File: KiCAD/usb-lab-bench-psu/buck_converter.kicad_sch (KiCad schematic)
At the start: 14 parts, among them U14 LMR16006X

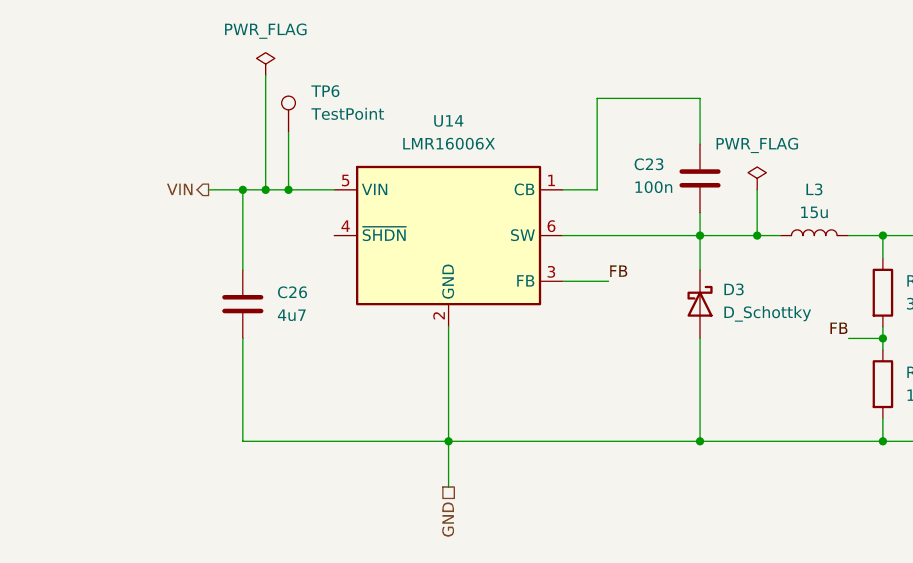
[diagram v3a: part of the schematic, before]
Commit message: restructured schematics to better show individual boards
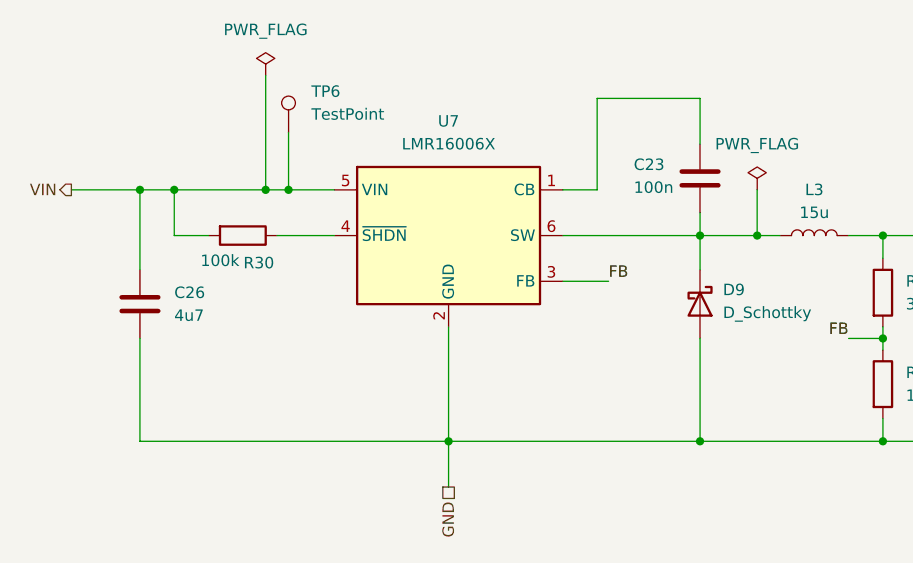
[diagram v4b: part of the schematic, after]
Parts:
- added R30: 100k, Resistor_SMD:R_0402_1005Metric_Pad0.72x0.64mm_HandSolder, symbol Device:R
- renumbered D3 to D9, U14 to U7
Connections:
- net VIN: now also R30.2
- net at U7.4 (~{SHDN}): now also R30.1
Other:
- moved on the sheet: C26
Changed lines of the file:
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@@
 	(paper "A4")
+	(junction
+		(at 71.12 71.12)
+		(diameter 0)
+		(color 0 0 0 0)
+	)
 	(junction
 		(at 81.28 71.12)
@@
 	)
 	(junction
-		(at 78.74 71.12)
+		(at 67.31 71.12)
 		(diameter 0)
 		(color 0 0 0 0)
@@
 	(wire
 		(pts
-			(xy 78.74 71.12) (xy 81.28 71.12)
-		)
-		(stroke
-			(width 0)
-			(type default)
-		)
-	)
-	(wire
-		(pts
 			(xy 83.82 71.12) (xy 88.9 71.12)
 		)
@@
 	(wire
 		(pts
-			(xy 78.74 71.12) (xy 78.74 80.01)
+			(xy 67.31 71.12) (xy 67.31 80.01)
 		)
 		(stroke
@@
 	(wire
 		(pts
+			(xy 67.31 71.12) (xy 71.12 71.12)
+		)
+		(stroke
+			(width 0)
+			(type default)
+		)
+	)
+	(wire
+		(pts
 			(xy 168.91 99.06) (xy 177.8 99.06)
 		)
@@
 	(wire
 		(pts
-			(xy 74.93 71.12) (xy 78.74 71.12)
-		)
-		(stroke
-			(width 0)
-			(type default)
-		)
-	)
-	(wire
-		(pts
 			(xy 190.5 99.06) (xy 190.5 95.25)
 		)
@@
 	(wire
 		(pts
-			(xy 78.74 99.06) (xy 101.6 99.06)
+			(xy 67.31 99.06) (xy 101.6 99.06)
 		)
 		(stroke
@@
 	(wire
 		(pts
+			(xy 59.69 71.12) (xy 67.31 71.12)
+		)
+		(stroke
+			(width 0)
+			(type default)
+		)
+	)
+	(wire
+		(pts
 			(xy 129.54 60.96) (xy 129.54 66.04)
 		)
@@
 	(wire
 		(pts
+			(xy 71.12 76.2) (xy 74.93 76.2)
+		)
+		(stroke
+			(width 0)
+			(type default)
+		)
+	)
+	(wire
+		(pts
 			(xy 149.86 96.52) (xy 149.86 99.06)
 		)
@@
 	(wire
 		(pts
+			(xy 82.55 76.2) (xy 88.9 76.2)
+		)
+		(stroke
+			(width 0)
+			(type default)
+		)
+	)
+	(wire
+		(pts
 			(xy 129.54 73.66) (xy 129.54 76.2)
 		)
@@
 	(wire
 		(pts
-			(xy 78.74 87.63) (xy 78.74 99.06)
+			(xy 67.31 87.63) (xy 67.31 99.06)
 		)
 		(stroke
@@
 		(pts
 			(xy 129.54 99.06) (xy 101.6 99.06)
+		)
+		(stroke
+			(width 0)
+			(type default)
+		)
+	)
+	(wire
+		(pts
+			(xy 71.12 71.12) (xy 81.28 71.12)
+		)
+		(stroke
+			(width 0)
+			(type default)
+		)
+	)
+	(wire
+		(pts
+			(xy 71.12 76.2) (xy 71.12 71.12)
 		)
 		(stroke
@@
 	(hierarchical_label "VIN"
 		(shape output)
-		(at 74.93 71.12 180)
+		(at 59.69 71.12 180)
 		(effects
 			(font
@@
 	(symbol
 		(lib_id "Device:C")
-		(at 78.74 83.82 0)
+		(at 67.31 83.82 0)
 		(unit 1)
 		(exclude_from_sim no)
@@
 		(fields_autoplaced yes)
 		(property "Reference" "C26"
-			(at 82.55 82.5499 0)
+			(at 71.12 82.5499 0)
 			(effects
 				(font
@@
 		)
 		(property "Value" "4u7"
-			(at 82.55 85.0899 0)
+			(at 71.12 85.0899 0)
 			(effects
 				(font
@@
 		)
 		(property "Footprint" ""
-			(at 79.7052 87.63 0)
+			(at 68.2752 87.63 0)
 			(effects
 				(font
@@
 		)
 		(property "Datasheet" "~"
-			(at 78.74 83.82 0)
+			(at 67.31 83.82 0)
 			(effects
 				(font
@@
 		)
 		(property "Description" "Unpolarized capacitor"
-			(at 78.74 83.82 0)
+			(at 67.31 83.82 0)
 			(effects
 				(font
@@
 		(instances
 			(project "usb-lab-bench-psu"
-				(path "/63928bc9-e618-488a-a687-c6d5597f31d9/7c3568f8-efef-4286-b162-68a5b336ac36"
-					(reference "C26")
+				(path "/63928bc9-e618-488a-a687-c6d5597f31d9/a793a91b-724b-4226-ba64-0dd946e3992c/5fb2809f-f6de-476a-bdb0-c9c28a070a75"
+					(reference "C61")
 					(unit 1)
 				)
@@
 		(instances
 			(project "usb-lab-bench-psu"
-				(path "/63928bc9-e618-488a-a687-c6d5597f31d9/7c3568f8-efef-4286-b162-68a5b336ac36"
-					(reference "TP7")
+				(path "/63928bc9-e618-488a-a687-c6d5597f31d9/a793a91b-724b-4226-ba64-0dd946e3992c/5fb2809f-f6de-476a-bdb0-c9c28a070a75"
+					(reference "TP13")
 					(unit 1)
 				)
@@
 		(instances
 			(project "usb-lab-bench-psu"
-				(path "/63928bc9-e618-488a-a687-c6d5597f31d9/7c3568f8-efef-4286-b162-68a5b336ac36"
-					(reference "D12")
+				(path "/63928bc9-e618-488a-a687-c6d5597f31d9/a793a91b-724b-4226-ba64-0dd946e3992c/5fb2809f-f6de-476a-bdb0-c9c28a070a75"
+					(reference "D13")
 					(unit 1)
 				)
@@
 		(instances
 			(project "usb-lab-bench-psu"
-				(path "/63928bc9-e618-488a-a687-c6d5597f31d9/7c3568f8-efef-4286-b162-68a5b336ac36"
-					(reference "#FLG010")
+				(path "/63928bc9-e618-488a-a687-c6d5597f31d9/a793a91b-724b-4226-ba64-0dd946e3992c/5fb2809f-f6de-476a-bdb0-c9c28a070a75"
+					(reference "#FLG014")
 					(unit 1)
 				)
@@
 		(instances
 			(project "usb-lab-bench-psu"
-				(path "/63928bc9-e618-488a-a687-c6d5597f31d9/7c3568f8-efef-4286-b162-68a5b336ac36"
-					(reference "R23")
+				(path "/63928bc9-e618-488a-a687-c6d5597f31d9/a793a91b-724b-4226-ba64-0dd946e3992c/5fb2809f-f6de-476a-bdb0-c9c28a070a75"
+					(reference "R37")
 					(unit 1)
 				)
@@
 		(instances
 			(project "usb-lab-bench-psu"
-				(path "/63928bc9-e618-488a-a687-c6d5597f31d9/7c3568f8-efef-4286-b162-68a5b336ac36"
-					(reference "TP6")
+				(path "/63928bc9-e618-488a-a687-c6d5597f31d9/a793a91b-724b-4226-ba64-0dd946e3992c/5fb2809f-f6de-476a-bdb0-c9c28a070a75"
+					(reference "TP5")
 					(unit 1)
 				)
@@
 		(instances
 			(project "usb-lab-bench-psu"
-				(path "/63928bc9-e618-488a-a687-c6d5597f31d9/7c3568f8-efef-4286-b162-68a5b336ac36"
-					(reference "C24")
+				(path "/63928bc9-e618-488a-a687-c6d5597f31d9/a793a91b-724b-4226-ba64-0dd946e3992c/5fb2809f-f6de-476a-bdb0-c9c28a070a75"
+					(reference "C66")
 					(unit 1)
 				)
@@
 		(instances
 			(project "usb-lab-bench-psu"
-				(path "/63928bc9-e618-488a-a687-c6d5597f31d9/7c3568f8-efef-4286-b162-68a5b336ac36"
-					(reference "R73")
+				(path "/63928bc9-e618-488a-a687-c6d5597f31d9/a793a91b-724b-4226-ba64-0dd946e3992c/5fb2809f-f6de-476a-bdb0-c9c28a070a75"
+					(reference "R39")
 					(unit 1)
 				)
@@
 		(instances
 			(project "usb-lab-bench-psu"
-				(path "/63928bc9-e618-488a-a687-c6d5597f31d9/7c3568f8-efef-4286-b162-68a5b336ac36"
-					(reference "C29")
+				(path "/63928bc9-e618-488a-a687-c6d5597f31d9/a793a91b-724b-4226-ba64-0dd946e3992c/5fb2809f-f6de-476a-bdb0-c9c28a070a75"
+					(reference "C65")
 					(unit 1)
 				)
@@
 		(instances
 			(project "usb-lab-bench-psu"
-				(path "/63928bc9-e618-488a-a687-c6d5597f31d9/7c3568f8-efef-4286-b162-68a5b336ac36"
-					(reference "C23")
+				(path "/63928bc9-e618-488a-a687-c6d5597f31d9/a793a91b-724b-4226-ba64-0dd946e3992c/5fb2809f-f6de-476a-bdb0-c9c28a070a75"
+					(reference "C62")
 					(unit 1)
 				)
@@
 		(dnp no)
 		(fields_autoplaced yes)
-		(property "Reference" "D3"
+		(property "Reference" "D9"
 			(at 132.08 82.2324 90)
 			(effects
@@
 		)
 		(instances
-			(project ""
-				(path "/63928bc9-e618-488a-a687-c6d5597f31d9/7c3568f8-efef-4286-b162-68a5b336ac36"
-					(reference "D3")
+			(project "usb-lab-bench-psu"
+				(path "/63928bc9-e618-488a-a687-c6d5597f31d9/a793a91b-724b-4226-ba64-0dd946e3992c/5fb2809f-f6de-476a-bdb0-c9c28a070a75"
+					(reference "D9")
 					(unit 1)
 				)
@@
 		(instances
 			(project "usb-lab-bench-psu"
-				(path "/63928bc9-e618-488a-a687-c6d5597f31d9/7c3568f8-efef-4286-b162-68a5b336ac36"
-					(reference "R24")
+				(path "/63928bc9-e618-488a-a687-c6d5597f31d9/a793a91b-724b-4226-ba64-0dd946e3992c/5fb2809f-f6de-476a-bdb0-c9c28a070a75"
+					(reference "R38")
 					(unit 1)
 				)
@@
 		(instances
 			(project "usb-lab-bench-psu"
-				(path "/63928bc9-e618-488a-a687-c6d5597f31d9/7c3568f8-efef-4286-b162-68a5b336ac36"
-					(reference "C25")
+				(path "/63928bc9-e618-488a-a687-c6d5597f31d9/a793a91b-724b-4226-ba64-0dd946e3992c/5fb2809f-f6de-476a-bdb0-c9c28a070a75"
+					(reference "C67")
 					(unit 1)
 				)
@@
 		(instances
 			(project "usb-lab-bench-psu"
-				(path "/63928bc9-e618-488a-a687-c6d5597f31d9/7c3568f8-efef-4286-b162-68a5b336ac36"
-					(reference "#FLG011")
+				(path "/63928bc9-e618-488a-a687-c6d5597f31d9/a793a91b-724b-4226-ba64-0dd946e3992c/5fb2809f-f6de-476a-bdb0-c9c28a070a75"
+					(reference "#FLG015")
+					(unit 1)
+				)
+			)
+		)
+	)
+	(symbol
+		(lib_id "Device:R")
+		(at 78.74 76.2 270)
+		(unit 1)
+		(exclude_from_sim no)
+		(in_bom yes)
+		(on_board yes)
+		(dnp no)
+		(property "Reference" "R30"
+			(at 80.518 79.248 90)
+			(effects
+				(font
+					(size 1.27 1.27)
+				)
+			)
+		)
+		(property "Value" "100k"
+			(at 76.2 78.994 90)
+			(effects
+				(font
+					(size 1.27 1.27)
+				)
+			)
+		)
+		(property "Footprint" "Resistor_SMD:R_0402_1005Metric_Pad0.72x0.64mm_HandSolder"
+			(at 78.74 74.422 90)
+			(effects
+				(font
+					(size 1.27 1.27)
+				)
+				(hide yes)
+			)
+		)
+		(property "Datasheet" "~"
+			(at 78.74 76.2 0)
+			(effects
+				(font
+					(size 1.27 1.27)
+				)
+				(hide yes)
+			)
+		)
+		(property "Description" ""
+			(at 78.74 76.2 0)
+			(effects
+				(font
+					(size 1.27 1.27)
+				)
+				(hide yes)
+			)
+		)
+		(pin "1"
+		)
+		(pin "2"
+		)
+		(instances
+			(project "usb-lab-bench-psu"
+				(path "/63928bc9-e618-488a-a687-c6d5597f31d9/a793a91b-724b-4226-ba64-0dd946e3992c/5fb2809f-f6de-476a-bdb0-c9c28a070a75"
+					(reference "R36")
 					(unit 1)
 				)
@@
 		(instances
 			(project "usb-lab-bench-psu"
-				(path "/63928bc9-e618-488a-a687-c6d5597f31d9/7c3568f8-efef-4286-b162-68a5b336ac36"
-					(reference "L3")
+				(path "/63928bc9-e618-488a-a687-c6d5597f31d9/a793a91b-724b-4226-ba64-0dd946e3992c/5fb2809f-f6de-476a-bdb0-c9c28a070a75"
+					(reference "L7")
 					(unit 1)
 				)
@@
 		(dnp no)
 		(fields_autoplaced yes)
-		(property "Reference" "U14"
+		(property "Reference" "U7"
 			(at 101.6 63.5 0)
 			(effects
@@
 		)
 		(instances
-			(project ""
-				(path "/63928bc9-e618-488a-a687-c6d5597f31d9/7c3568f8-efef-4286-b162-68a5b336ac36"
-					(reference "U14")
+			(project "usb-lab-bench-psu"
+				(path "/63928bc9-e618-488a-a687-c6d5597f31d9/a793a91b-724b-4226-ba64-0dd946e3992c/5fb2809f-f6de-476a-bdb0-c9c28a070a75"
+					(reference "U7")
 					(unit 1)
 				)

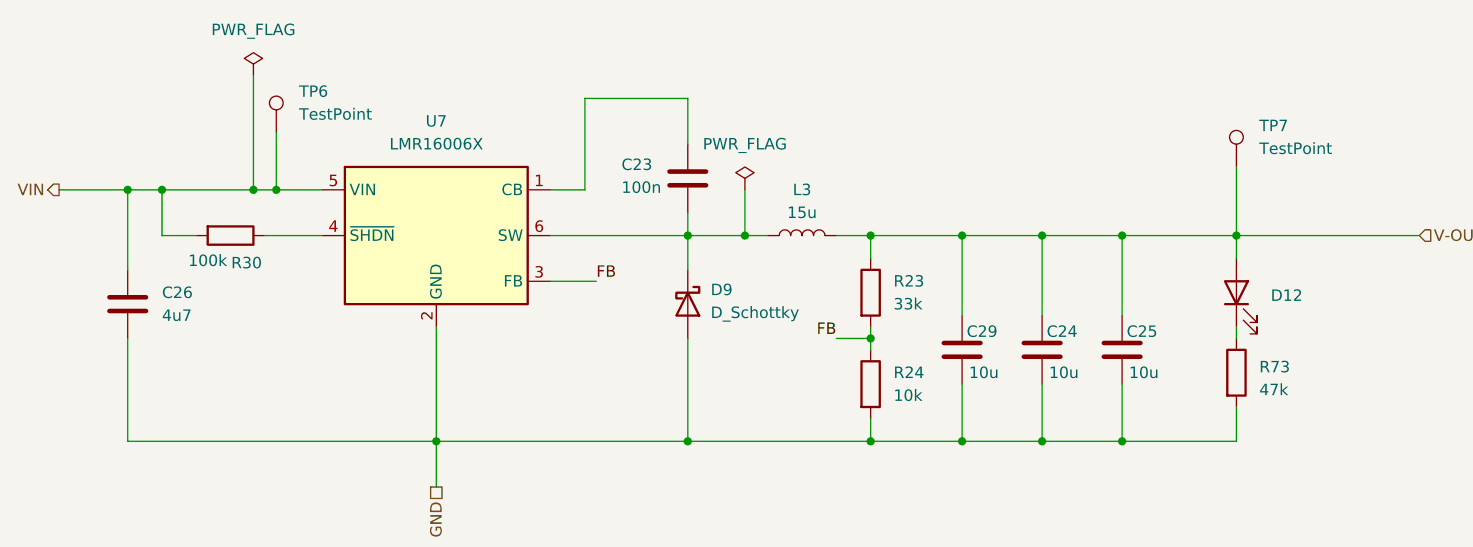
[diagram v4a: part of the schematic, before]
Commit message: updated spi for display
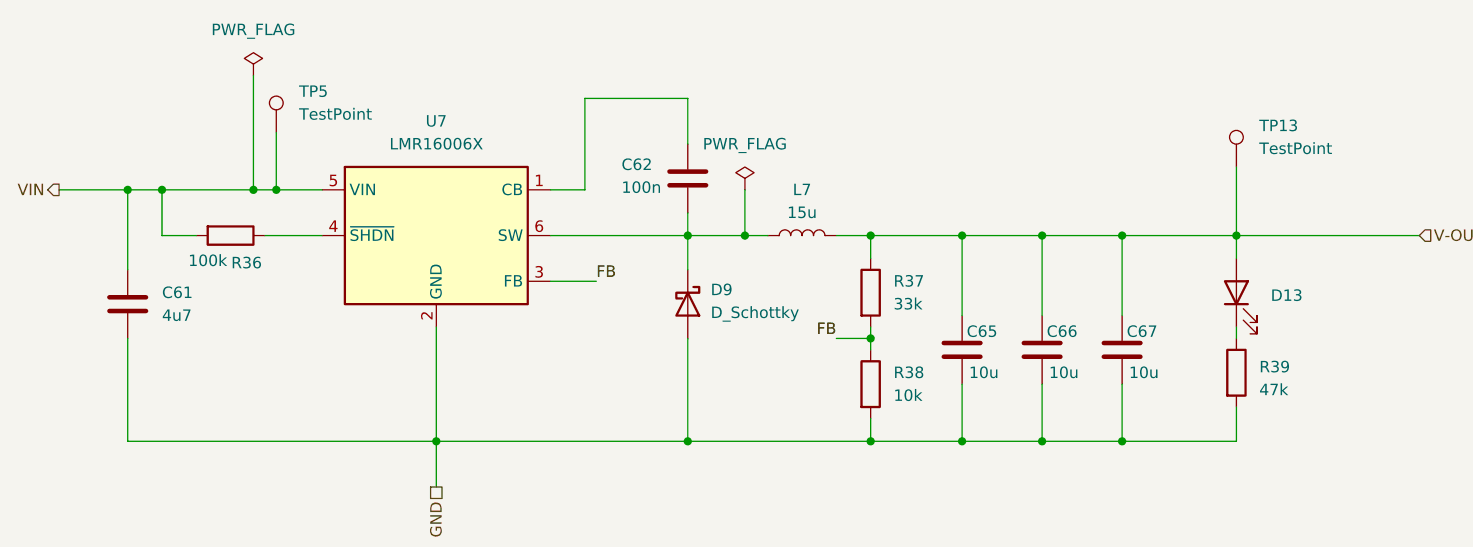
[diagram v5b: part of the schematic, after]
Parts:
- renumbered C26 to C61, C23 to C62, C29 to C65, C24 to C66, C25 to C67, D12 to D13, L3 to L7, R30 to R36, R23 to R37, R24 to R38, R73 to R39, TP7 to TP13, TP6 to TP5
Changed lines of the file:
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@@
 		(dnp no)
 		(fields_autoplaced yes)
-		(property "Reference" "C26"
+		(property "Reference" "C61"
 			(at 71.12 82.5499 0)
 			(effects
@@
 		(dnp no)
 		(fields_autoplaced yes)
-		(property "Reference" "TP7"
+		(property "Reference" "TP13"
 			(at 193.04 64.0079 0)
 			(effects
@@
 		(dnp no)
 		(fields_autoplaced yes)
-		(property "Reference" "D12"
+		(property "Reference" "D13"
 			(at 194.31 82.8674 90)
 			(effects
@@
 		(dnp no)
 		(fields_autoplaced yes)
-		(property "Reference" "#FLG010"
+		(property "Reference" "#FLG014"
 			(at 81.28 56.515 0)
 			(effects
@@
 		(dnp no)
 		(fields_autoplaced yes)
-		(property "Reference" "R23"
+		(property "Reference" "R37"
 			(at 152.4 81.2799 0)
 			(effects
@@
 		(dnp no)
 		(fields_autoplaced yes)
-		(property "Reference" "TP6"
+		(property "Reference" "TP5"
 			(at 86.36 60.1979 0)
 			(effects
@@
 		(on_board yes)
 		(dnp no)
-		(property "Reference" "C24"
+		(property "Reference" "C66"
 			(at 169.418 86.868 0)
 			(effects
@@
 		(dnp no)
 		(fields_autoplaced yes)
-		(property "Reference" "R73"
+		(property "Reference" "R39"
 			(at 193.04 90.805 0)
 			(effects
@@
 		(on_board yes)
 		(dnp no)
-		(property "Reference" "C29"
+		(property "Reference" "C65"
 			(at 160.528 86.868 0)
 			(effects
@@
 		(on_board yes)
 		(dnp no)
-		(property "Reference" "C23"
+		(property "Reference" "C62"
 			(at 122.174 68.326 0)
 			(effects
@@
 		(dnp no)
 		(fields_autoplaced yes)
-		(property "Reference" "R24"
+		(property "Reference" "R38"
 			(at 152.4 91.4399 0)
 			(effects
@@
 		(on_board yes)
 		(dnp no)
-		(property "Reference" "C25"
+		(property "Reference" "C67"
 			(at 178.308 86.868 0)
 			(effects
@@
 		(dnp no)
 		(fields_autoplaced yes)
-		(property "Reference" "#FLG011"
+		(property "Reference" "#FLG015"
 			(at 135.89 69.215 0)
 			(effects
@@
 		(on_board yes)
 		(dnp no)
-		(property "Reference" "R30"
+		(property "Reference" "R36"
 			(at 80.518 79.248 90)
 			(effects
@@
 		(dnp no)
 		(fields_autoplaced yes)
-		(property "Reference" "L3"
+		(property "Reference" "L7"
 			(at 142.24 71.12 90)
 			(effects

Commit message: added current limiting circuit for USB PD sink, added 2nd buck converter
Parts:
- removed C61: 4u7, symbol Device:C
- removed C62: 100n, symbol Device:C
- removed C65, C66, C67: 10u, symbol Device:C
- removed D13: XL-1005UGC, Diode_SMD:D_0402_1005Metric_Pad0.77x0.64mm_HandSolder, symbol Device:LED
- removed D9: D_Schottky, symbol Device:D_Schottky
- removed L7: 15u, symbol Device:L
- removed R36: 100k, Resistor_SMD:R_0402_1005Metric_Pad0.72x0.64mm_HandSolder, symbol Device:R
- removed R37: 33k, Resistor_SMD:R_0402_1005Metric_Pad0.72x0.64mm_HandSolder, symbol Device:R
- removed R38: 10k, Resistor_SMD:R_0402_1005Metric_Pad0.72x0.64mm_HandSolder, symbol Device:R
- removed R39: 47k, Resistor_SMD:R_0402_1005Metric_Pad0.72x0.64mm_HandSolder, symbol Device:R
- removed TP13, TP5: TestPoint, symbol Connector:TestPoint
- removed U7: LMR16006X, Package_TO_SOT_SMD:TSOT-23-6, symbol Prj_dcdc_converter:LMR16006X
